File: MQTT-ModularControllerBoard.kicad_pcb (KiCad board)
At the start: 4 copper layers, 200 x 45 mm, 83 parts, among them IC301 LM74700QDBVTQ1, IC401 TLV76733DRVR, IC403 LM74700QDBVTQ1, J301 1715721, J501 A2541HWV-10P, J502 A2541HWV-10P, J503 A2541HWV-10P, J504 A2541HWV-10P, J505 A2541HWV-10P, J506 A2541HWV-10P, J507 A2541HWV-10P, J508 A2541HWV-10P, J601 1051640001, Q301 60V 38A, Q402 60V 38A, U201 ESP32-S3-WROOM-1U-N16R8, U601 ESD Protection IC

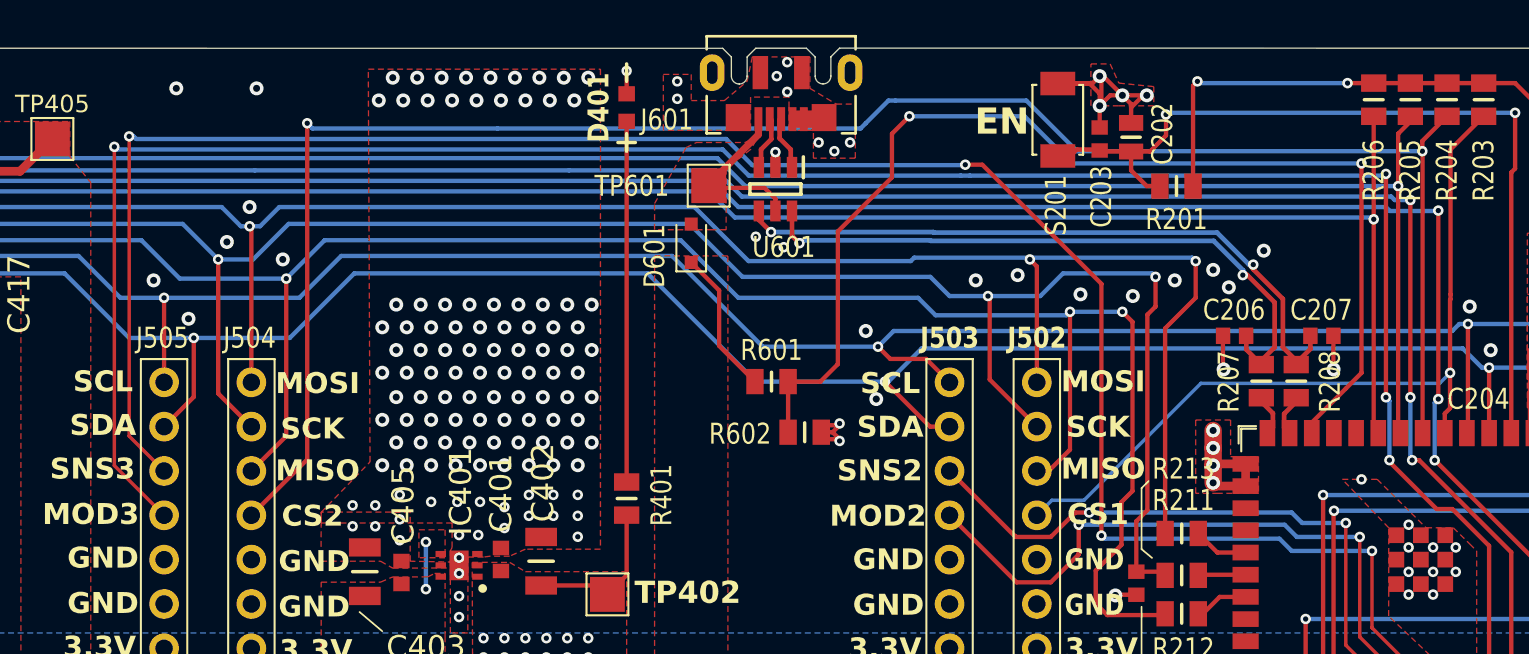
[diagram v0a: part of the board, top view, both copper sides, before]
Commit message: Adjusted trace layout to separate GPIO43 and GPIO44 to help prevent crosstalk in case of attempting manual flashing.
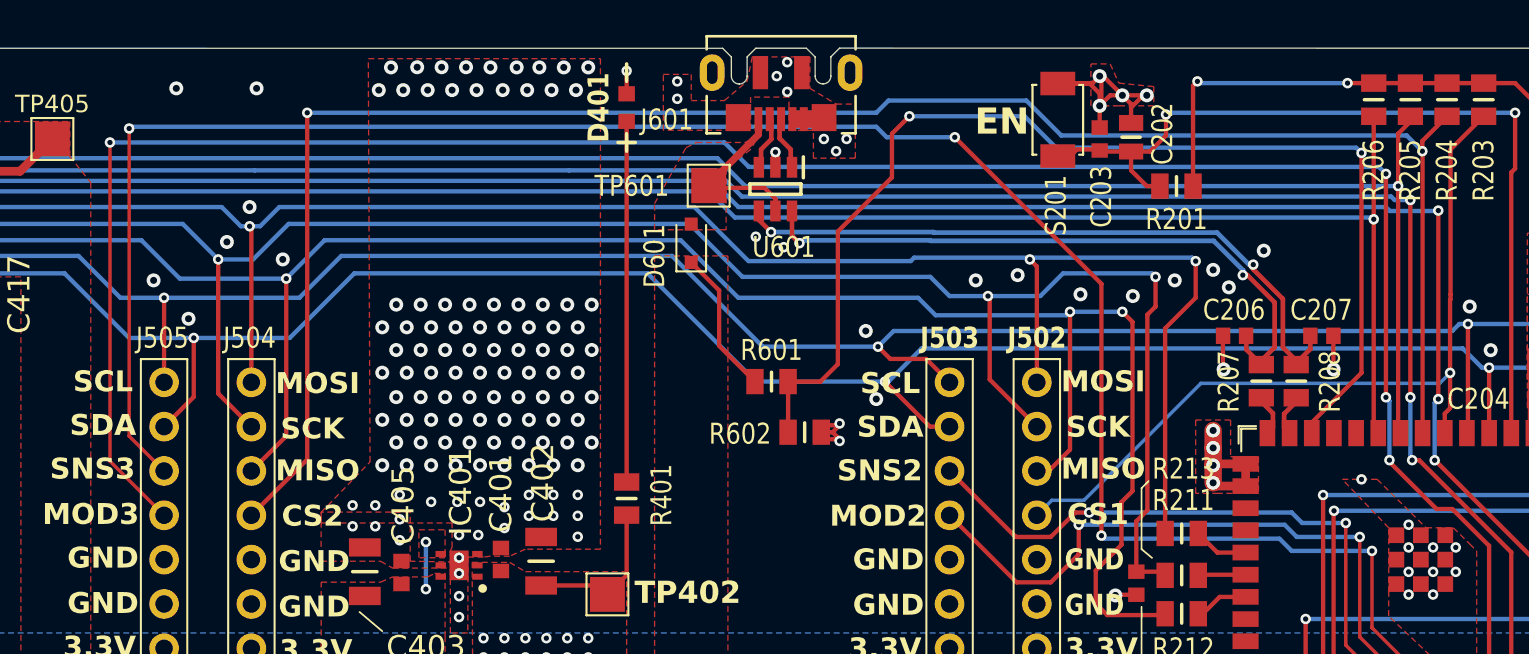
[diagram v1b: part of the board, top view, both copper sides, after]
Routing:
- net /ESP32-S3/SENSE3: track 122.6 -> 123.2 mm
- net /ESP32-S3/MOD3: track 131.2 -> 131.8 mm

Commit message: Silkscreen tweaks for polarity.
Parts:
- added ?: , clipboard:cab4aadf-0fde-4372-9020-6eb9f3107f87, F.Cu at (227.0, 113.3)
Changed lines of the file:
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@@
 			(layer "F.SilkS")
 		)
+		(fp_circle
+			(center -2.1 0)
+			(end -2.1 0.1)
+			(stroke
+				(width 0.1)
+				(type solid)
+			)
+			(fill yes)
+			(layer "F.SilkS")
+		)
 		(fp_line
 			(start 1.2 -1.1)
@@
 			(layer "F.SilkS")
 		)
+		(fp_circle
+			(center -2.425 -0.9)
+			(end -2.425 -0.775)
+			(stroke
+				(width 0.25)
+				(type solid)
+			)
+			(fill no)
+			(layer "F.SilkS")
+		)
 		(fp_line
 			(start -1.2 1.8)
@@
 			(layer "F.SilkS")
 		)
+		(fp_circle
+			(center -2.425 -0.9)
+			(end -2.425 -0.775)
+			(stroke
+				(width 0.25)
+				(type solid)
+			)
+			(fill no)
+			(layer "F.SilkS")
+		)
 		(fp_line
 			(start -2.1 -1.8)
@@
 		)
 	)
+	(footprint "clipboard:cab4aadf-0fde-4372-9020-6eb9f3107f87"
+		(layer "F.Cu")
+		(at 227 113.3)
+		(property "Reference" ""
+			(at 0 0 0)
+			(layer "F.SilkS")
+			(effects
+				(font
+					(size 1.27 1.27)
+					(thickness 0.15)
+				)
+			)
+		)
+		(property "Value" ""
+			(at 0 0 0)
+			(layer "F.Fab")
+			(effects
+				(font
+					(size 1.27 1.27)
+					(thickness 0.15)
+				)
+			)
+		)
+		(property "Datasheet" ""
+			(at 0 0 0)
+			(layer "F.Fab")
+			(hide yes)
+			(effects
+				(font
+					(size 1.27 1.27)
+					(thickness 0.15)
+				)
+			)
+		)
+		(property "Description" ""
+			(at 0 0 0)
+			(layer "F.Fab")
+			(hide yes)
+			(effects
+				(font
+					(size 1.27 1.27)
+					(thickness 0.15)
+				)
+			)
+		)
+		(fp_circle
+			(center -0.125 0)
+			(end -0.125 0.125)
+			(stroke
+				(width 0.25)
+				(type solid)
+			)
+			(fill no)
+			(layer "F.SilkS")
+		)
+		(embedded_fonts no)
+	)
 	(footprint "JLCPCB Basic:CAPC1608X90N"
 		(layer "F.Cu")
@@
 			(layer "F.SilkS")
 		)
+		(fp_circle
+			(center -2.4 -0.9)
+			(end -2.4 -0.775)
+			(stroke
+				(width 0.25)
+				(type solid)
+			)
+			(fill no)
+			(layer "F.SilkS")
+		)
 		(fp_line
 			(start -2.125 -1.8)
@@
 		(tags "Integrated Circuit")
 		(property "Reference" "IC403"
-			(at -3.2 0 180)
+			(at -3.8 0 180)
 			(layer "F.SilkS")
 			(effects
@@
 			(layer "F.SilkS")
 		)
+		(fp_circle
+			(center -2.425 -0.9)
+			(end -2.425 -0.775)
+			(stroke
+				(width 0.25)
+				(type solid)
+			)
+			(fill no)
+			(layer "F.SilkS")
+		)
 		(fp_line
 			(start 1.1 -1.8)
@@
 		(tags "Capacitor")
 		(property "Reference" "C201"
-			(at -0.5 -1.9 0)
+			(at 0 2 0)
 			(layer "F.SilkS")
 			(effects

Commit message: Updated Fab layer and silkscreen.
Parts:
- removed ?: , clipboard:cab4aadf-0fde-4372-9020-6eb9f3107f87
- H101, H102, H103, H104: value MountingHole 3.5mm -> 3.5mm
- U201: footprint PCM_Espressif:ESP32-S3-WROOM-1U -> ESPRESSIF Microcontrollers:ESP32-S3-WROOM-1U
